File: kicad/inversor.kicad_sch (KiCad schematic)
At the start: 64 parts, among them J1 VCC, J2 PWM, J3 LCD 16x2, J4 MainFan, J5 380VFreed, J6 PRO_MINI_L, J7 PRO_MINI_T, J8 PRO_MINI_R, Q1 SSF6014D, Q2 TIP120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

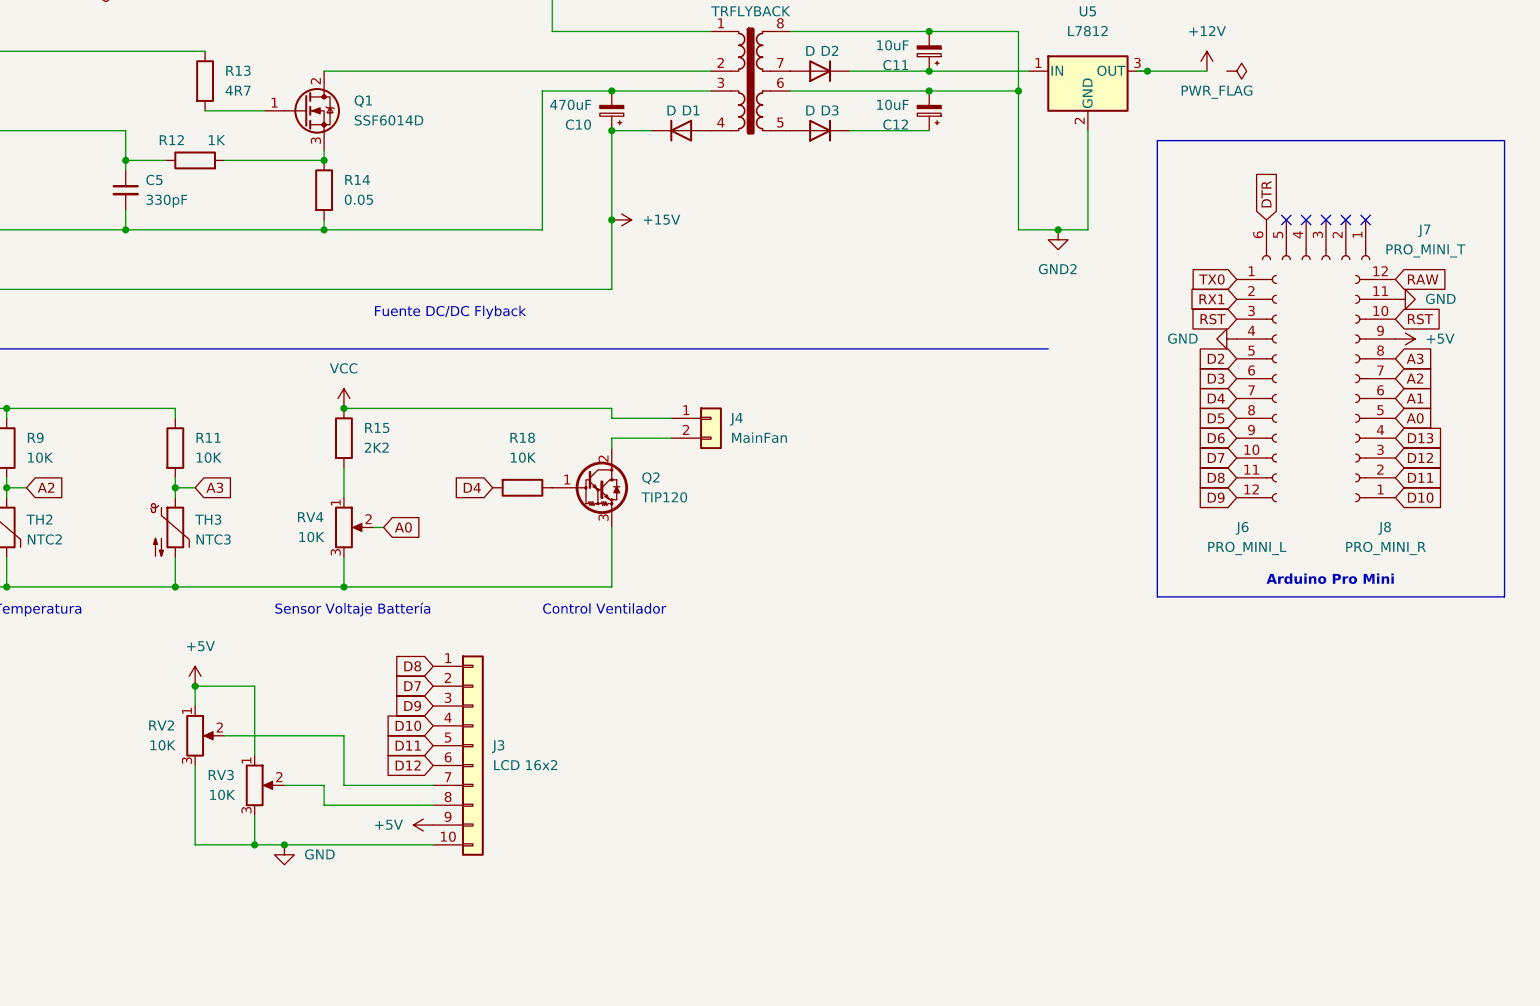
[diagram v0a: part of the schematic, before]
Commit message: Cambio Arduino por el ATMega328
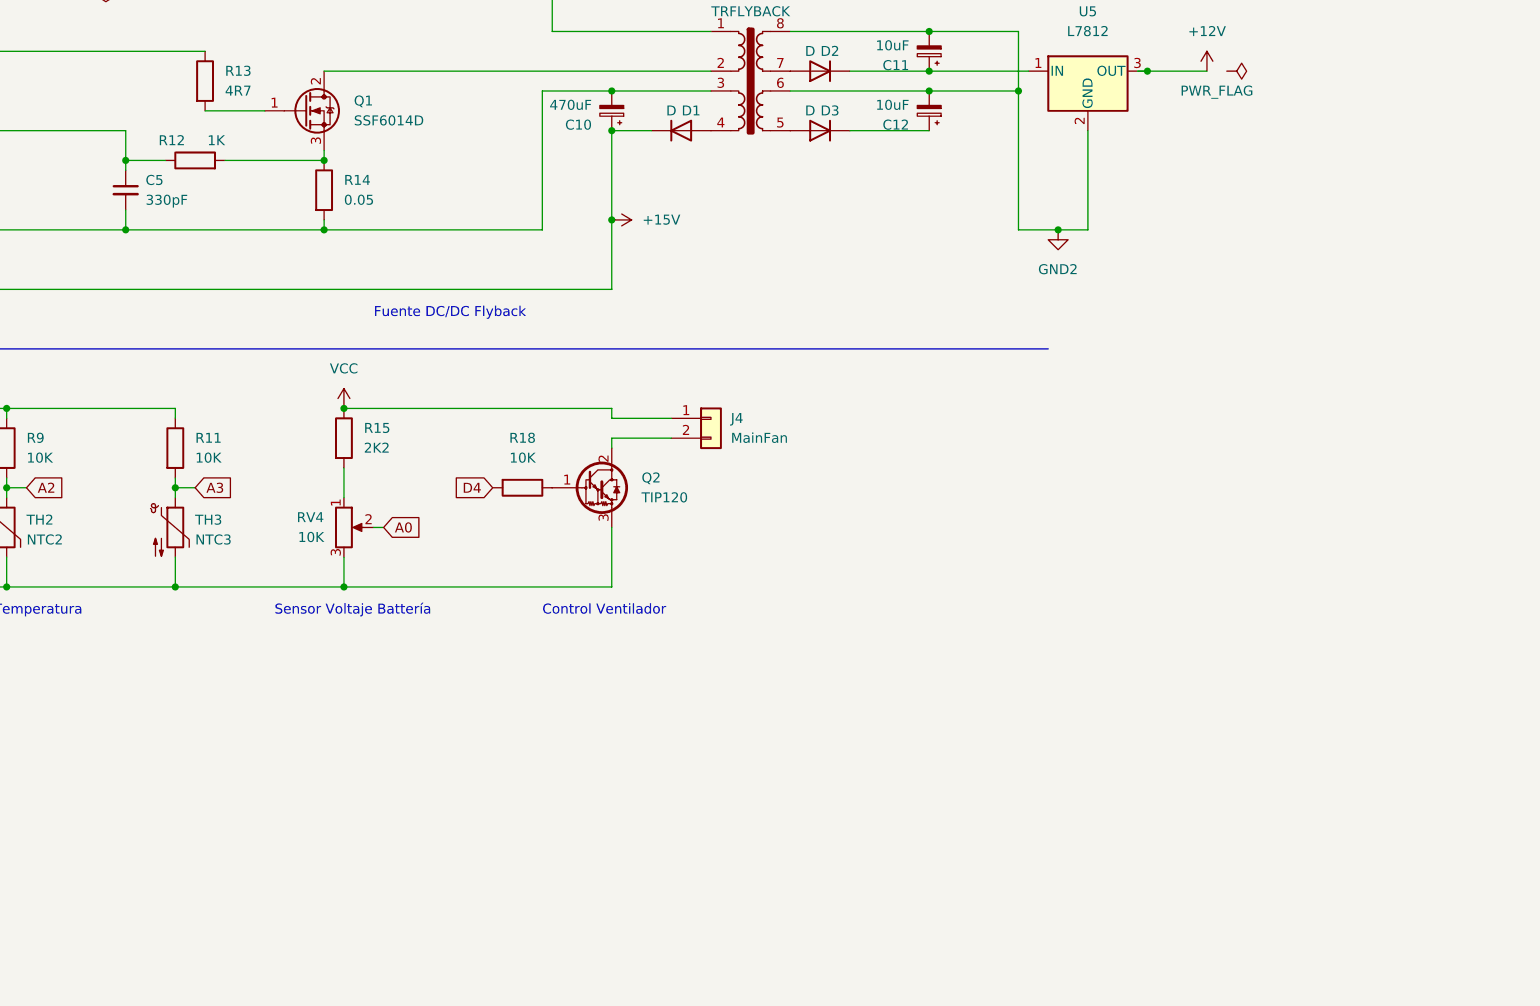
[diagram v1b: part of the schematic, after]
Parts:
- removed J3: LCD 16x2, Connector_PinSocket_2.54mm:PinSocket_1x10_P2.54mm_Vertical, symbol Connector_Generic:Conn_01x10
- removed J6: PRO_MINI_L, Connector_PinSocket_2.54mm:PinSocket_1x12_P2.54mm_Vertical, symbol Connector:Conn_01x12_Female
- removed J7: PRO_MINI_T, Connector_PinSocket_2.54mm:PinSocket_1x06_P2.54mm_Vertical, symbol Connector:Conn_01x06_Female
- removed J8: PRO_MINI_R, Connector_PinSocket_2.54mm:PinSocket_1x12_P2.54mm_Vertical, symbol Connector:Conn_01x12_Female
- removed RV2, RV3: 10K, Potentiometer_THT:Potentiometer_Bourns_3296W_Vertical, symbol Device:R_Potentiometer
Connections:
- no-connect marks 7 -> 2
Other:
- note removed: "Arduino Pro Mini"
